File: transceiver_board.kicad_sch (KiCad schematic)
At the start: 0 parts

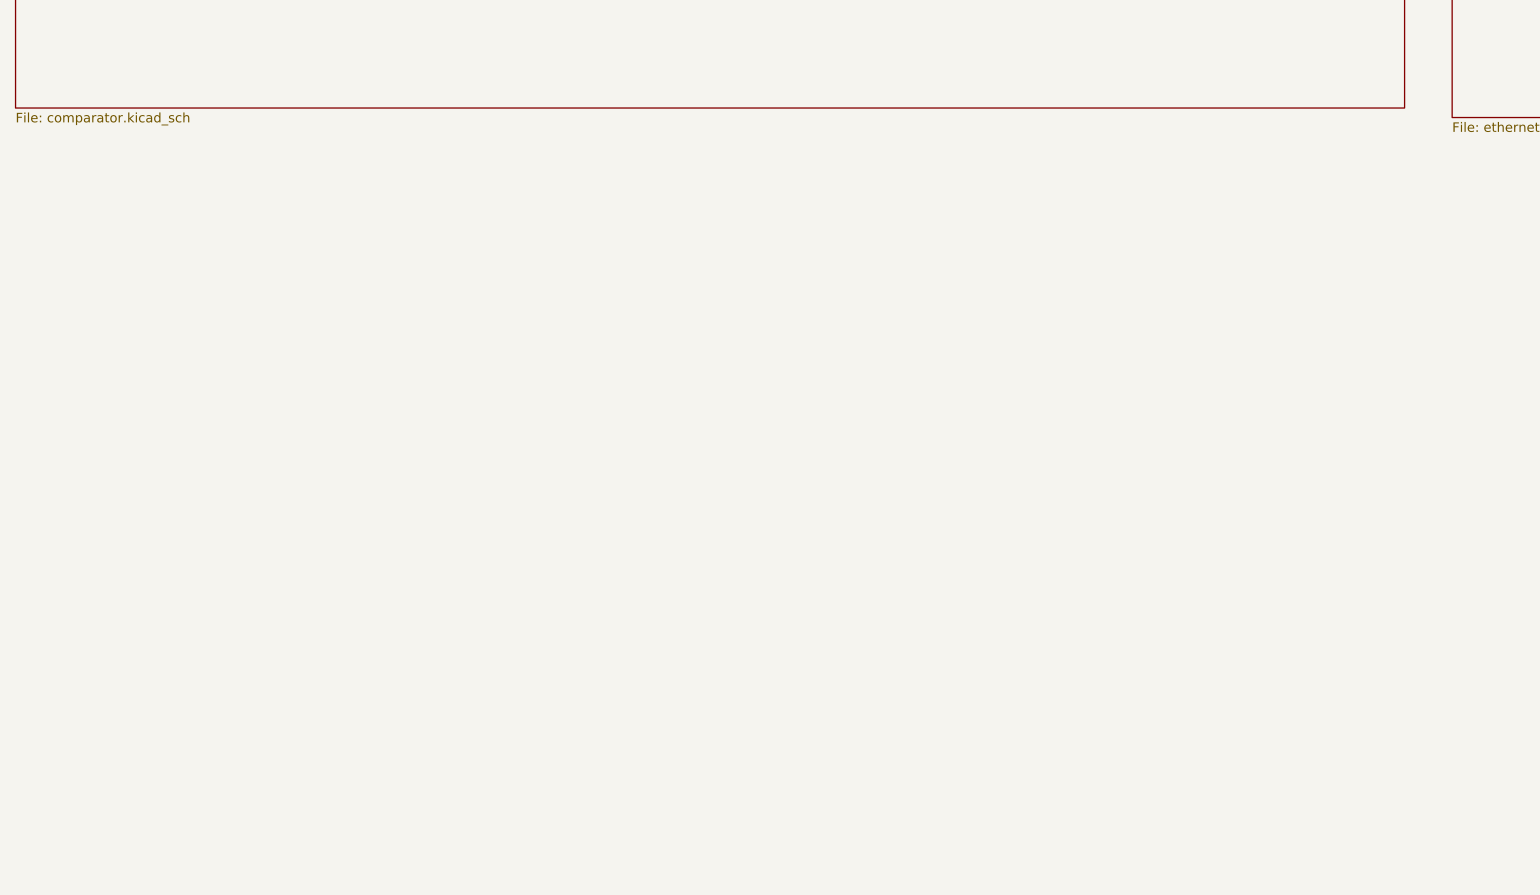
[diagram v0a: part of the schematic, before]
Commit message: Add photo transmitter to main sheet
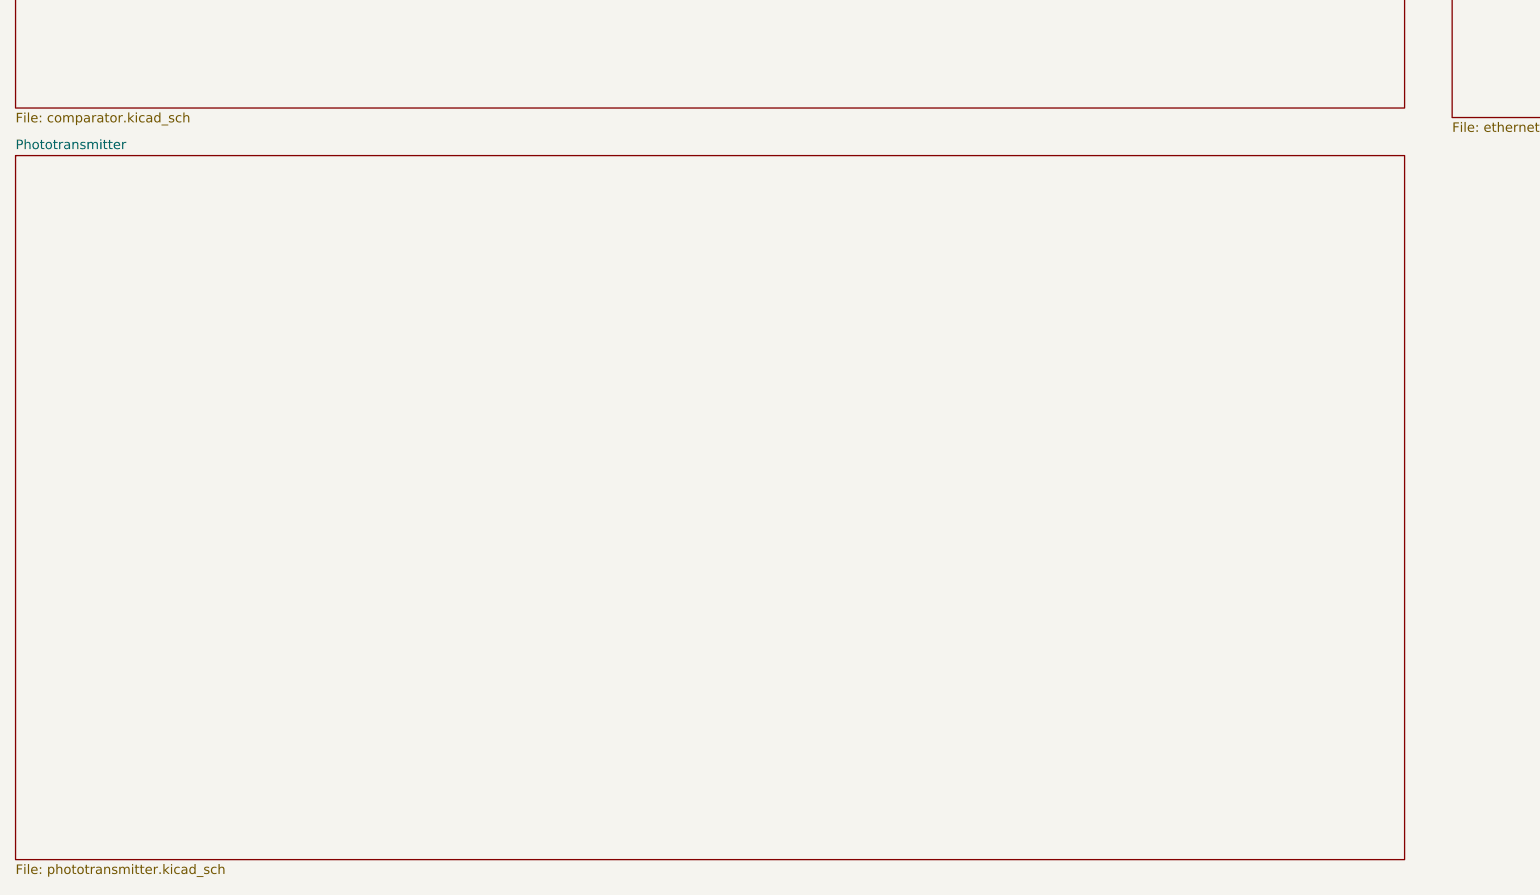
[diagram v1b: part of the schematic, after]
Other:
- added sheet Phototransmitter (phototransmitter.kicad_sch)
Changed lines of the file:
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@@
+    )
+  )
+  (sheet (at 16.51 250.19) (size 185.42 93.98) (fields_autoplaced)
+    (stroke (width 0.1524) (type solid) (color 0 0 0 0))
+    (fill (color 0 0 0 0.0000))
+    (property "Sheet name" "Phototransmitter" (id 0) (at 16.51 249.4784 0)
+      (effects (font (size 1.27 1.27)) (justify left bottom))
+    )
+    (property "Sheet file" "phototransmitter.kicad_sch" (id 1) (at 16.51 344.7546 0)
+      (effects (font (size 1.27 1.27)) (justify left top))
     )
   )
@@
     (path "/ba74941e-d0cd-46a4-ade7-f1aec57ffafc" (page "6"))
     (path "/9c91d18d-68d4-4932-8503-e5dad9f3ecb3" (page "7"))
+    (path "/7439cf31-4a35-4348-9fd9-f17e5e75d79c" (page "8"))
   )
   (symbol_instances

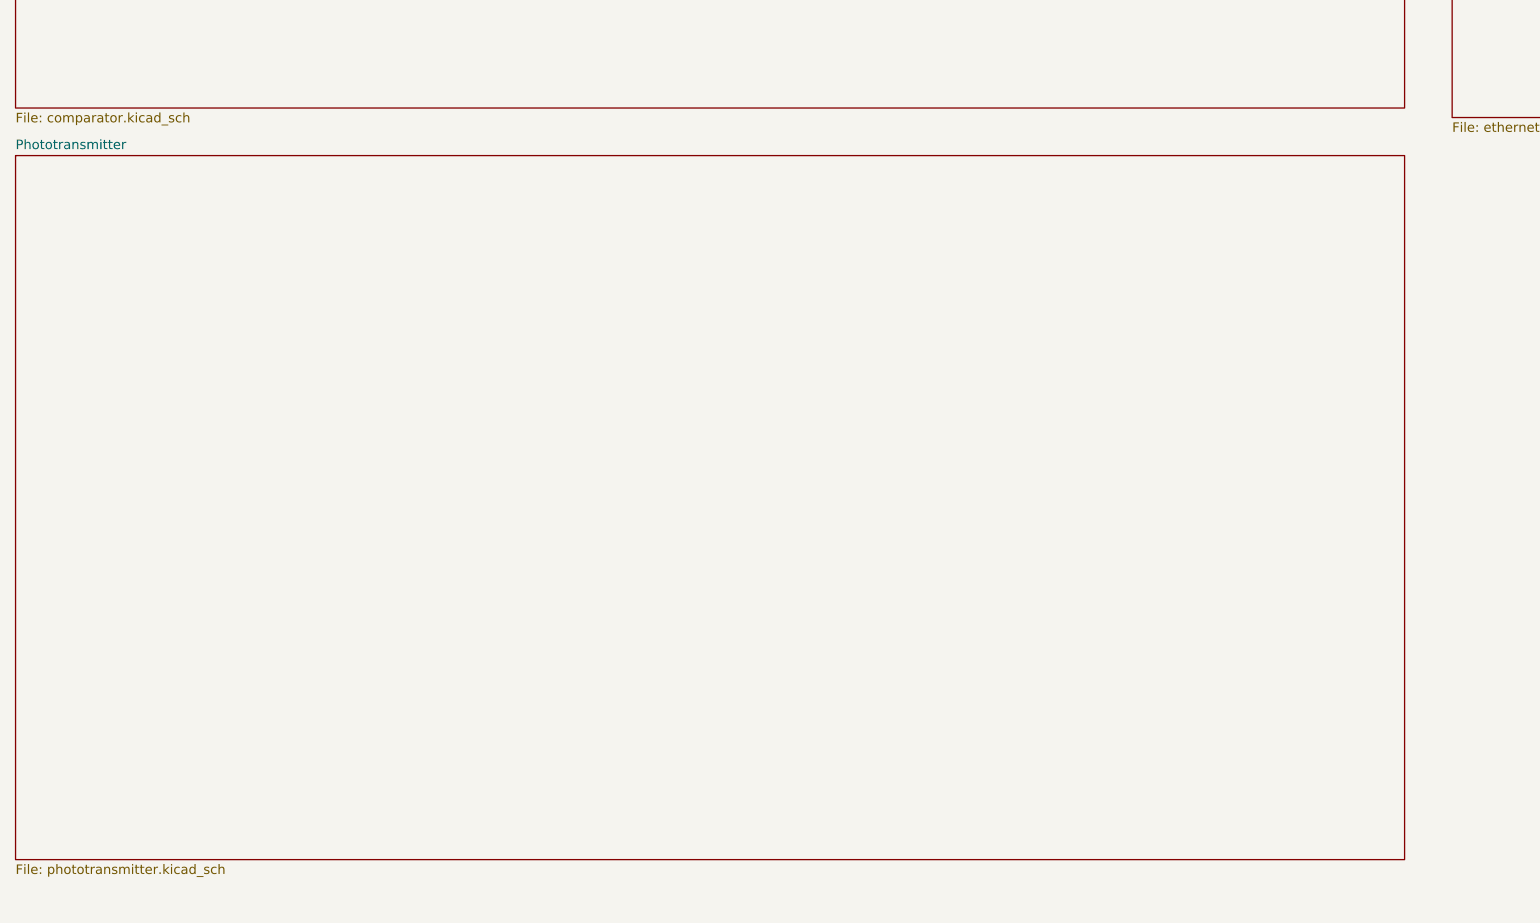
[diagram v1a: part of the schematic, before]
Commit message: Added power supply and standardised on pwer supply net names
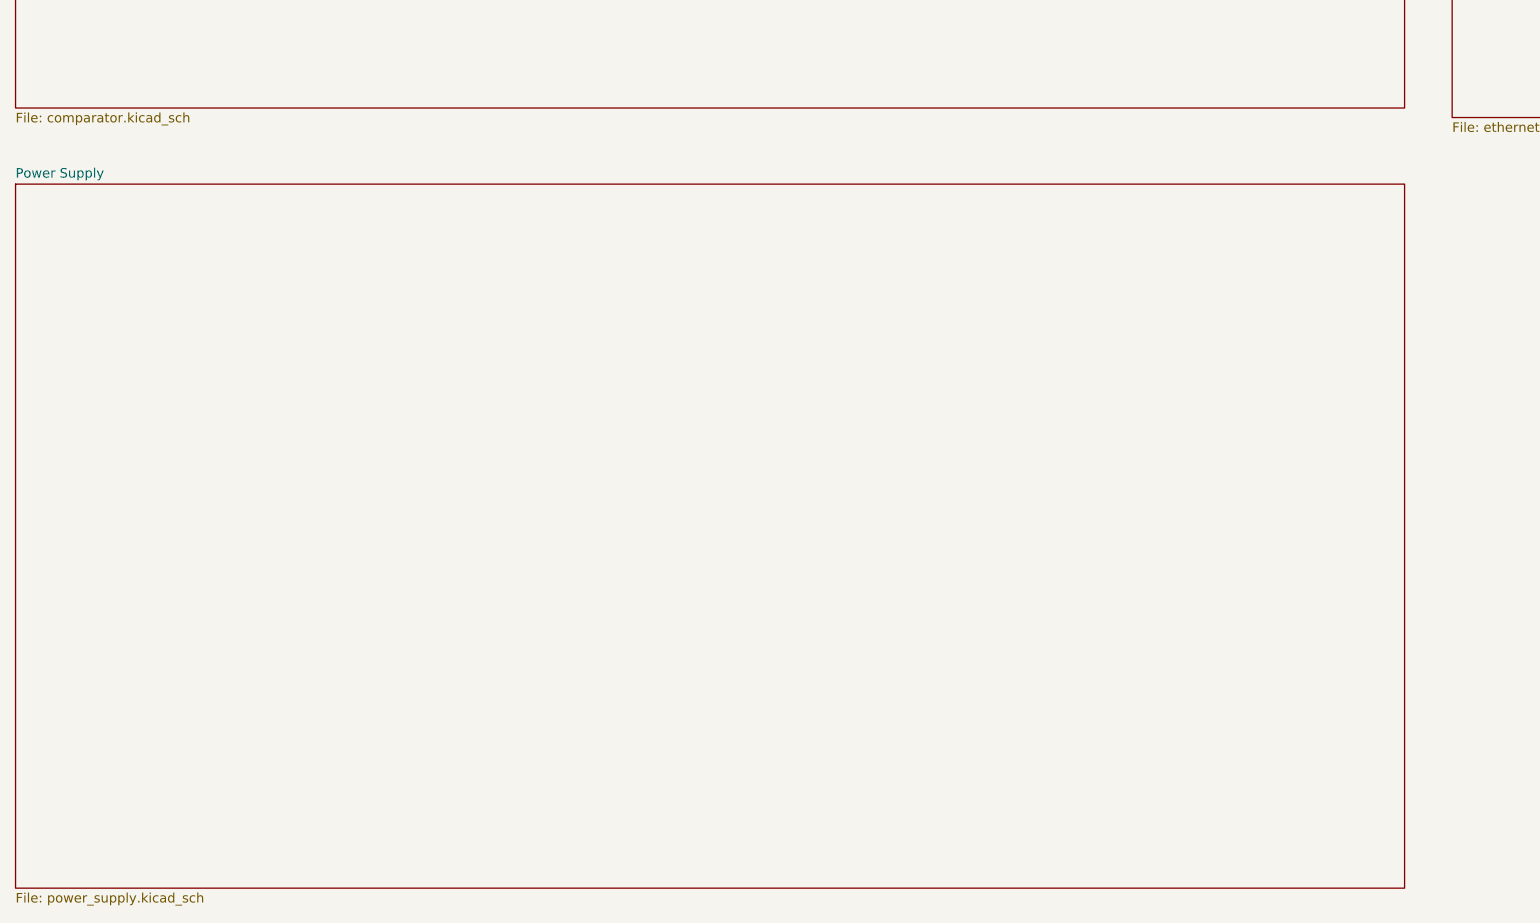
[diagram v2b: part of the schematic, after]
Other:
- removed sheet Phototransmitter
- added sheet Power Supply (power_supply.kicad_sch)
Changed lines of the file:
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@@
 (kicad_sch (version 20211123) (generator eeschema)
   (paper "A2")
+  (sheet (at 16.51 254) (size 185.42 93.98) (fields_autoplaced)
+    (stroke (width 0.1524) (type solid) (color 0 0 0 0))
+    (fill (color 0 0 0 0.0000))
+    (property "Sheet name" "Power Supply" (id 0) (at 16.51 253.2884 0)
+      (effects (font (size 1.27 1.27)) (justify left bottom))
+    )
+    (property "Sheet file" "power_supply.kicad_sch" (id 1) (at 16.51 348.5646 0)
+      (effects (font (size 1.27 1.27)) (justify left top))
+    )
+  )
   (sheet (at 16.51 16.51) (size 185.42 114.3) (fields_autoplaced)
     (stroke (width 0.1524) (type solid) (color 0 0 0 0))
@@
     )
     (property "Sheet file" "comparator.kicad_sch" (id 1) (at 16.51 244.4246 0)
-      (effects (font (size 1.27 1.27)) (justify left top))
-    )
-  )
-  (sheet (at 16.51 250.19) (size 185.42 93.98) (fields_autoplaced)
-    (stroke (width 0.1524) (type solid) (color 0 0 0 0))
-    (fill (color 0 0 0 0.0000))
-    (property "Sheet name" "Phototransmitter" (id 0) (at 16.51 249.4784 0)
-      (effects (font (size 1.27 1.27)) (justify left bottom))
-    )
-    (property "Sheet file" "phototransmitter.kicad_sch" (id 1) (at 16.51 344.7546 0)
       (effects (font (size 1.27 1.27)) (justify left top))
     )
@@
     (path "/ba74941e-d0cd-46a4-ade7-f1aec57ffafc" (page "6"))
     (path "/9c91d18d-68d4-4932-8503-e5dad9f3ecb3" (page "7"))
-    (path "/7439cf31-4a35-4348-9fd9-f17e5e75d79c" (page "8"))
+    (path "/099fbc0b-58f5-4ea0-91be-48e4a94d6545" (page "8"))
   )
   (symbol_instances
@@
       (reference "#PWR?") (unit 1) (value "GND1") (footprint "")
     )
+    (path "/099fbc0b-58f5-4ea0-91be-48e4a94d6545/0cf8851d-d06a-4093-b522-b5a4af3e86e6"
+      (reference "#PWR?") (unit 1) (value "GND") (footprint "")
+    )
     (path "/8e682951-d8d0-4614-a72d-99ac2c01b394/0edf2349-be6c-4e0c-8c9f-79c0afd1c644"
       (reference "#PWR?") (unit 1) (value "GND") (footprint "")
     )
+    (path "/9252f6c6-964c-4a99-bc96-7468213f7a97/188affc5-3ce9-44cf-870c-ac3bba725e98"
+      (reference "#PWR?") (unit 1) (value "GND") (footprint "")
+    )
     (path "/51bba4f8-4ea3-409a-8f3c-dd75ae3bfb55/1a8b304b-45e5-49bb-aa50-edadc02513e4"
       (reference "#PWR?") (unit 1) (value "GND") (footprint "")
@@
     (path "/8e682951-d8d0-4614-a72d-99ac2c01b394/30c0f81d-150a-48b1-b84a-de4012116686"
       (reference "#PWR?") (unit 1) (value "GND") (footprint "")
+    )
+    (path "/099fbc0b-58f5-4ea0-91be-48e4a94d6545/315fbd9d-d8f0-4f15-801f-0464f3682cb7"
+      (reference "#PWR?") (unit 1) (value "+5V") (footprint "")
     )
     (path "/9c91d18d-68d4-4932-8503-e5dad9f3ecb3/333ededc-6193-4b81-8c10-b8e504d96e63"
@@
       (reference "#PWR?") (unit 1) (value "GND1") (footprint "")
     )
+    (path "/099fbc0b-58f5-4ea0-91be-48e4a94d6545/7c59fc9b-2490-45f1-b63c-8f9e8804f3da"
+      (reference "#PWR?") (unit 1) (value "+12V") (footprint "")
+    )
     (path "/8e682951-d8d0-4614-a72d-99ac2c01b394/81f5f9c0-c086-44f6-8b78-766eff9a0822"
       (reference "#PWR?") (unit 1) (value "+3V3") (footprint "")
@@
       (reference "#PWR?") (unit 1) (value "+3V3") (footprint "")
     )
+    (path "/099fbc0b-58f5-4ea0-91be-48e4a94d6545/babe0bf8-9b6d-4d29-b1a5-2c7281f175ef"
+      (reference "#PWR?") (unit 1) (value "+3V3") (footprint "")
+    )
     (path "/8e682951-d8d0-4614-a72d-99ac2c01b394/bf1c6056-3ff9-48ba-b820-7a09167957a0"
       (reference "#PWR?") (unit 1) (value "GND") (footprint "")
@@
       (reference "#PWR?") (unit 1) (value "GND") (footprint "")
     )
+    (path "/099fbc0b-58f5-4ea0-91be-48e4a94d6545/c8ece296-11c4-4674-82ed-1bc5a8264bac"
+      (reference "#PWR?") (unit 1) (value "GND") (footprint "")
+    )
     (path "/8e682951-d8d0-4614-a72d-99ac2c01b394/cbb79b60-c885-4873-a89e-9da01d68cfc2"
       (reference "#PWR?") (unit 1) (value "GND") (footprint "")
@@
     )
     (path "/8e682951-d8d0-4614-a72d-99ac2c01b394/d404f433-5b18-4a6a-9f7f-1767cc932c3b"
+      (reference "#PWR?") (unit 1) (value "GND") (footprint "")
+    )
+    (path "/099fbc0b-58f5-4ea0-91be-48e4a94d6545/d8d5bf3e-2efe-48ef-b283-15225815d120"
       (reference "#PWR?") (unit 1) (value "GND") (footprint "")
     )
@@
       (reference "#PWR?") (unit 1) (value "GND1") (footprint "")
     )
+    (path "/9252f6c6-964c-4a99-bc96-7468213f7a97/e755f76f-d654-43ec-9d56-6b639def1538"
+      (reference "#PWR?") (unit 1) (value "+5V") (footprint "")
+    )
     (path "/8e682951-d8d0-4614-a72d-99ac2c01b394/ea9e07f4-709b-4bd8-8963-938def869674"
       (reference "#PWR?") (unit 1) (value "GND") (footprint "")
+    )
+    (path "/ba74941e-d0cd-46a4-ade7-f1aec57ffafc/f2b1bbd6-aa07-4df3-91d8-0863e6b16891"
+      (reference "#PWR?") (unit 1) (value "+5V") (footprint "")
     )
     (path "/ba74941e-d0cd-46a4-ade7-f1aec57ffafc/37390626-ae04-4360-9ff8-4cc9e030e613"
@@
       (reference "C?") (unit 1) (value "0.022uF") (footprint "")
     )
+    (path "/099fbc0b-58f5-4ea0-91be-48e4a94d6545/2e906deb-f6f9-49b0-8f88-53512d5fec05"
+      (reference "C?") (unit 1) (value "100nF") (footprint "")
+    )
     (path "/8e682951-d8d0-4614-a72d-99ac2c01b394/31c9a0ca-f42c-4826-ad73-e5110ef3047b"
       (reference "C?") (unit 1) (value "3.3uF") (footprint "")
@@
       (reference "C?") (unit 1) (value "3.3uF") (footprint "")
     )
+    (path "/099fbc0b-58f5-4ea0-91be-48e4a94d6545/3a06562f-d9ba-4770-ae9f-bf388e63253e"
+      (reference "C?") (unit 1) (value "100nF") (footprint "")
+    )
+    (path "/099fbc0b-58f5-4ea0-91be-48e4a94d6545/45a3ca22-013c-4a89-b38c-b05893fee138"
+      (reference "C?") (unit 1) (value "22uF") (footprint "")
+    )
     (path "/51bba4f8-4ea3-409a-8f3c-dd75ae3bfb55/45ac3d35-0e07-40e3-b2f6-1daee7c64de7"
       (reference "C?") (unit 1) (value "2u2") (footprint "")
@@
       (reference "C?") (unit 1) (value "0.1uF") (footprint "")
     )
+    (path "/099fbc0b-58f5-4ea0-91be-48e4a94d6545/6d5b33d3-0d96-4830-8842-96db1f6f8216"
+      (reference "C?") (unit 1) (value "10uF") (footprint "")
+    )
     (path "/51bba4f8-4ea3-409a-8f3c-dd75ae3bfb55/7a7faf29-9736-40de-9707-4410dc4e29cd"
       (reference "C?") (unit 1) (value "100n") (footprint "")
@@
       (reference "C?") (unit 1) (value "0.1uF") (footprint "")
     )
+    (path "/099fbc0b-58f5-4ea0-91be-48e4a94d6545/912dfcd8-5566-4747-b281-d4e0e1b65920"
+      (reference "C?") (unit 1) (value "10uF") (footprint "")
+    )
     (path "/8e682951-d8d0-4614-a72d-99ac2c01b394/93437cb1-2abe-4632-b41e-b01142ae1c78"
       (reference "C?") (unit 1) (value "0.1uF") (footprint "")
@@
       (reference "C?") (unit 1) (value "3.3uF") (footprint "")
     )
+    (path "/099fbc0b-58f5-4ea0-91be-48e4a94d6545/a98b32d4-e12f-4e03-a785-2329d24f2ad6"
+      (reference "C?") (unit 1) (value "22uF") (footprint "")
+    )
     (path "/51bba4f8-4ea3-409a-8f3c-dd75ae3bfb55/aaa0908f-ac48-4471-a2be-8f6cd57d7370"
       (reference "C?") (unit 1) (value "100n") (footprint "")
@@
       (reference "C?") (unit 1) (value "0.1uF") (footprint "")
     )
+    (path "/099fbc0b-58f5-4ea0-91be-48e4a94d6545/b4720e09-60ce-4416-9ce4-768f3be25dc0"
+      (reference "C?") (unit 1) (value "22uF") (footprint "")
+    )
     (path "/9c91d18d-68d4-4932-8503-e5dad9f3ecb3/beed6f73-49f4-4c04-9e72-0f76bb642acc"
       (reference "C?") (unit 1) (value "6.8nF") (footprint "")
     )
+    (path "/099fbc0b-58f5-4ea0-91be-48e4a94d6545/ca5290c3-e303-49b6-8ae4-4933817dfd58"
+      (reference "C?") (unit 1) (value "22uF") (footprint "")
+    )
     (path "/9c91d18d-68d4-4932-8503-e5dad9f3ecb3/d98737d6-8bf3-4547-844e-a96b8cbb7494"
       (reference "C?") (unit 1) (value "0.022uF") (footprint "")
@@
       (reference "C_noise") (unit 1) (value "0.1u") (footprint "")
     )
+    (path "/9252f6c6-964c-4a99-bc96-7468213f7a97/215d754c-1940-4430-b670-e74952280409"
+      (reference "D?") (unit 1) (value "D_Schottky") (footprint "")
+    )
     (path "/8e682951-d8d0-4614-a72d-99ac2c01b394/ad95eee4-50d1-4e47-9a36-397876ebec9f"
       (reference "D?") (unit 1) (value "LED") (footprint "")
@@
       (reference "FPGA?") (unit 1) (value "Artix-7 Dev Board") (footprint "")
     )
+    (path "/099fbc0b-58f5-4ea0-91be-48e4a94d6545/34254c17-7c32-4c88-873b-e0a530efa838"
+      (reference "J?") (unit 1) (value "Conn_01x02_Male") (footprint "")
+    )
     (path "/2ed4948e-59e2-4bfe-884a-1c527b3a5f14/baa84674-ad20-4613-871a-531aac59e40e"
       (reference "J?") (unit 1) (value "RJ45_LED_Shielded") (footprint "")
@@
       (reference "JP?") (unit 1) (value "SolderJumper_2_Open") (footprint "")
     )
+    (path "/099fbc0b-58f5-4ea0-91be-48e4a94d6545/751536b1-8094-435f-a749-58b392d63f26"
+      (reference "L?") (unit 1) (value "2.2uH") (footprint "")
+    )
+    (path "/099fbc0b-58f5-4ea0-91be-48e4a94d6545/f83cff11-12c1-4b3f-89dd-61de0bb46b7e"
+      (reference "L?") (unit 1) (value "2.2uH") (footprint "")
+    )
     (path "/ba74941e-d0cd-46a4-ade7-f1aec57ffafc/584ec624-a8dc-44ac-8701-d12fd00a4c29"
       (reference "PhotoReceiver") (unit 1) (value "FDS010") (footprint "")
@@
       (reference "U?") (unit 1) (value "AD8014ARZ") (footprint "SOIC127P600X175-8N")
     )
+    (path "/099fbc0b-58f5-4ea0-91be-48e4a94d6545/6b2071d9-6b48-47d7-8601-73d02a3549ec"
+      (reference "U?") (unit 1) (value "AP63205WU") (footprint "Package_TO_SOT_SMD:TSOT-23-6")
+    )
     (path "/51bba4f8-4ea3-409a-8f3c-dd75ae3bfb55/72b49ec8-c68f-4d04-913b-fe685e96edee"
       (reference "U?") (unit 1) (value "ltc6752ims8-2-pbf") (footprint "MSOP-8_MS")
     )
+    (path "/099fbc0b-58f5-4ea0-91be-48e4a94d6545/e666d43a-ae22-40a6-8ab9-492b56f71406"
+      (reference "U?") (unit 1) (value "AP63203WU") (footprint "Package_TO_SOT_SMD:TSOT-23-6")
+    )
     (path "/8e682951-d8d0-4614-a72d-99ac2c01b394/e688799b-e7ea-44b5-88bf-b31cf54751af"
